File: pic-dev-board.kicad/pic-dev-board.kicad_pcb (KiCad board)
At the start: 2 copper layers, 100 x 100 mm, 0 parts

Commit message: initial pcb-layout, no traces yet
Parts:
- added ?: , , F.Cu at (34.5, 33.3)
- added C1: 100n, Capacitor_THT:C_Disc_D3.0mm_W2.0mm_P2.50mm, F.Cu at (54.0, 49.0)
- added D1: LED, user:LED_1206_3216_Pad1.7x1.75mm_BB, F.Cu at (109.2, 71.4)
- added D10: LED, user:LED_1206_3216_Pad1.7x1.75mm_BB, F.Cu at (82.0, 71.4)
- added D11: LED, user:LED_1206_3216_Pad1.7x1.75mm_BB, F.Cu at (79.5, 71.4)
- added D12: LED, user:LED_1206_3216_Pad1.7x1.75mm_BB, F.Cu at (77.0, 71.4)
- added D13: LED, user:LED_1206_3216_Pad1.7x1.75mm_BB, F.Cu at (74.4, 71.4)
- added D14: LED, user:LED_1206_3216_Pad1.7x1.75mm_BB, F.Cu at (71.9, 71.4)
- added D15: LED, user:LED_1206_3216_Pad1.7x1.75mm_BB, F.Cu at (65.8, 71.4)
- added D16: LED, user:LED_1206_3216_Pad1.7x1.75mm_BB, F.Cu at (63.2, 71.4)
- added D17: LED, user:LED_1206_3216_Pad1.7x1.75mm_BB, F.Cu at (60.7, 71.4)
- added D18: LED, user:LED_1206_3216_Pad1.7x1.75mm_BB, F.Cu at (58.2, 71.4)
- added D19: LED, user:LED_1206_3216_Pad1.7x1.75mm_BB, F.Cu at (55.6, 71.4)
- added D2: LED, user:LED_1206_3216_Pad1.7x1.75mm_BB, F.Cu at (109.2, 82.8)
- added D20: LED, user:LED_1206_3216_Pad1.7x1.75mm_BB, F.Cu at (53.2, 71.4)
- added D21: LED, user:LED_1206_3216_Pad1.7x1.75mm_BB, F.Cu at (50.5, 71.4)
- added D22: LED, user:LED_1206_3216_Pad1.7x1.75mm_BB, F.Cu at (48.0, 71.4)
- added D3: LED, user:LED_1206_3216_Pad1.7x1.75mm_BB, F.Cu at (109.2, 75.2)
- added D4: LED, user:LED_1206_3216_Pad1.7x1.75mm_BB, F.Cu at (109.2, 86.6)
- added D5: LED, user:LED_1206_3216_Pad1.7x1.75mm_BB, F.Cu at (109.2, 79.0)
- added D6: D_Schottky, Diode_THT:D_A-405_P7.62mm_Horizontal, F.Cu at (46.5, 55.1)
- added D7: LED, user:LED_1206_3216_Pad1.7x1.75mm_BB, F.Cu at (89.7, 71.4)
- added D8: LED, user:LED_1206_3216_Pad1.7x1.75mm_BB, F.Cu at (87.1, 71.4)
- added D9: LED, user:LED_1206_3216_Pad1.7x1.75mm_BB, F.Cu at (84.6, 71.4)
- added DS1: WC1602A, user:WC1602A_Connector, F.Cu at (47.0, 34.1)
- added J1: Conn_GP0, Connector_PinHeader_2.54mm:PinHeader_1x03_P2.54mm_Vertical, F.Cu at (99.6, 71.4)
- added J10: Jumper DATin, Connector_PinHeader_2.54mm:PinHeader_1x02_P2.54mm_Vertical, F.Cu at (96.5, 59.7)
- added J11: Conn_SR_2, Connector_PinHeader_2.54mm:PinHeader_1x08_P2.54mm_Vertical, F.Cu at (65.8, 87.4)
- added J12: Conn_SR_1, Connector_PinHeader_2.54mm:PinHeader_1x08_P2.54mm_Vertical, F.Cu at (89.7, 87.4)
- added J13: Conn_5V_GND, Connector_PinHeader_2.54mm:PinHeader_2x15_P2.54mm_Vertical, F.Cu at (80.8, 91.2)
- added J14: Jumper CLKin, Connector_PinHeader_2.54mm:PinHeader_1x02_P2.54mm_Vertical, F.Cu at (89.9, 59.4)
- added J15: Barrel_Jack_Switch, Connector_BarrelJack:BarrelJack_CUI_PJ-102AH_Horizontal, F.Cu at (44.0, 99.0)
- added J16: RUN/~PGM, Connector_PinHeader_2.54mm:PinHeader_1x02_P2.54mm_Vertical, F.Cu at (33.3, 56.0)
- added J17: I2C, Connector_PinHeader_2.54mm:PinHeader_1x04_P2.54mm_Vertical, F.Cu at (33.1, 64.0)
- added J18: GP1(RA1)/RB6, Connector_PinHeader_2.54mm:PinHeader_1x03_P2.54mm_Vertical, F.Cu at (59.0, 59.0)
- added J19: GP2(RA2)/RB4, Connector_PinHeader_2.54mm:PinHeader_1x03_P2.54mm_Vertical, F.Cu at (72.0, 59.0)
- added J2: Conn_GP4, Connector_PinHeader_2.54mm:PinHeader_1x03_P2.54mm_Vertical, F.Cu at (99.6, 82.8)
- added J3: Conn_GP1, Connector_PinHeader_2.54mm:PinHeader_1x03_P2.54mm_Vertical, F.Cu at (99.6, 75.2)
- added J4: Conn_GP5, Connector_PinHeader_2.54mm:PinHeader_1x03_P2.54mm_Vertical, F.Cu at (99.6, 86.6)
- added J5: Conn_GP2, Connector_PinHeader_2.54mm:PinHeader_1x03_P2.54mm_Vertical, F.Cu at (99.6, 79.0)
- added J6: Conn_ICSP, Connector_PinHeader_2.54mm:PinHeader_1x06_P2.54mm_Vertical, F.Cu at (33.3, 39.3)
- added J7: Conn_TRISC, Connector_PinHeader_2.54mm:PinHeader_1x10_P2.54mm_Vertical, F.Cu at (126.2, 97.8)
- added J8: Conn_TRISA, Connector_PinHeader_2.54mm:PinHeader_1x07_P2.54mm_Vertical, F.Cu at (126.2, 59.2)
- added J9: Conn_TRISB, Connector_PinHeader_2.54mm:PinHeader_1x06_P2.54mm_Vertical, F.Cu at (126.2, 79.8)
- added R1: 4.7k, user:R_1206_3216_Pad1.7x1.75mm_BB, F.Cu at (94.5, 71.4)
- added R10: 1k, user:R_1206_3216_Pad1.7x1.75mm_BB, F.Cu at (114.8, 79.0)
- added R11: 1k, user:R_1206_3216_Pad1.7x1.75mm_BB, F.Cu at (43.4, 52.8)
- added R12: 22k, user:R_1206_3216_Pad1.7x1.75mm_BB, F.Cu at (48.5, 51.8)
- added R13: 1k, user:R_1206_3216_Pad1.7x1.75mm_BB, F.Cu at (48.5, 48.5)
- added R14: 1k, user:R_1206_3216_Pad1.7x1.75mm_BB, F.Cu at (52.8, 45.0)
- added R15: 220, user:R_1206_3216_Pad1.7x1.75mm_BB, F.Cu at (90.4, 34.0)
- added R16: 4.7k, user:R_1206_3216_Pad1.7x1.75mm_BB, F.Cu at (36.6, 70.6)
- added R17: 4.7k, user:R_1206_3216_Pad1.7x1.75mm_BB, F.Cu at (36.6, 65.0)
- added R2: 1k, user:R_1206_3216_Pad1.7x1.75mm_BB, F.Cu at (114.8, 71.4)
- added R3: 4.7k, user:R_1206_3216_Pad1.7x1.75mm_BB, F.Cu at (94.5, 82.8)
- added R4: 1k, user:R_1206_3216_Pad1.7x1.75mm_BB, F.Cu at (114.8, 82.8)
- added R5: 4.7k, user:R_1206_3216_Pad1.7x1.75mm_BB, F.Cu at (94.5, 75.2)
- added R6: 1k, user:R_1206_3216_Pad1.7x1.75mm_BB, F.Cu at (114.8, 75.2)
- added R7: 4.7k, user:R_1206_3216_Pad1.7x1.75mm_BB, F.Cu at (94.5, 86.6)
- added R8: 1k, user:R_1206_3216_Pad1.7x1.75mm_BB, F.Cu at (114.8, 86.6)
- added R9: 4.7k, user:R_1206_3216_Pad1.7x1.75mm_BB, F.Cu at (94.5, 79.0)
- added REF**: Proto_Area_13x15_P2.54mm_Drill1.0mm, Proto_Area:Proto_Area_13x15, F.Cu at (85.9, 91.2)
- added REF**: Proto_Area_13x15_P2.54mm_Drill1.0mm, Proto_Area:Proto_Area_13x15, F.Cu at (47.8, 91.2)
- added REF**: MountingHole_2.7mm_M2.5, MountingHole:MountingHole_2.7mm_M2.5, F.Cu at (126.7, 33.3)
- added REF**: MountingHole_2.7mm_M2.5, MountingHole:MountingHole_2.7mm_M2.5, F.Cu at (126.7, 126.7)
- added REF**: MountingHole_2.7mm_M2.5, MountingHole:MountingHole_2.7mm_M2.5, F.Cu at (33.3, 126.7)
- added REF**: MountingHole_2.7mm_M2.5, MountingHole:MountingHole_2.7mm_M2.5, F.Cu at (33.3, 33.3)
- added RN1: 680, Resistor_THT:R_Array_SIP9, F.Cu at (92.2, 64.8)
- added RN2: 680, Resistor_THT:R_Array_SIP9, F.Cu at (68.3, 64.8)
- added RV1: 10K, Potentiometer_THT:Potentiometer_Bourns_3386X_Horizontal, F.Cu at (126.0, 49.0)
- added SW1: SW_Push, Button_Switch_THT:SW_PUSH_6mm_H9.5mm, F.Cu at (33.3, 90.9)
- added U1: PIC16F690-IP, Package_DIP:DIP-20_W7.62mm_Socket, F.Cu at (58.0, 53.0)
- added U2: 74HC595, Package_DIP:DIP-16_W7.62mm_Socket, F.Cu at (89.7, 76.2)
- added U3: 74HC595, Package_DIP:DIP-16_W7.62mm_Socket, F.Cu at (65.8, 76.2)

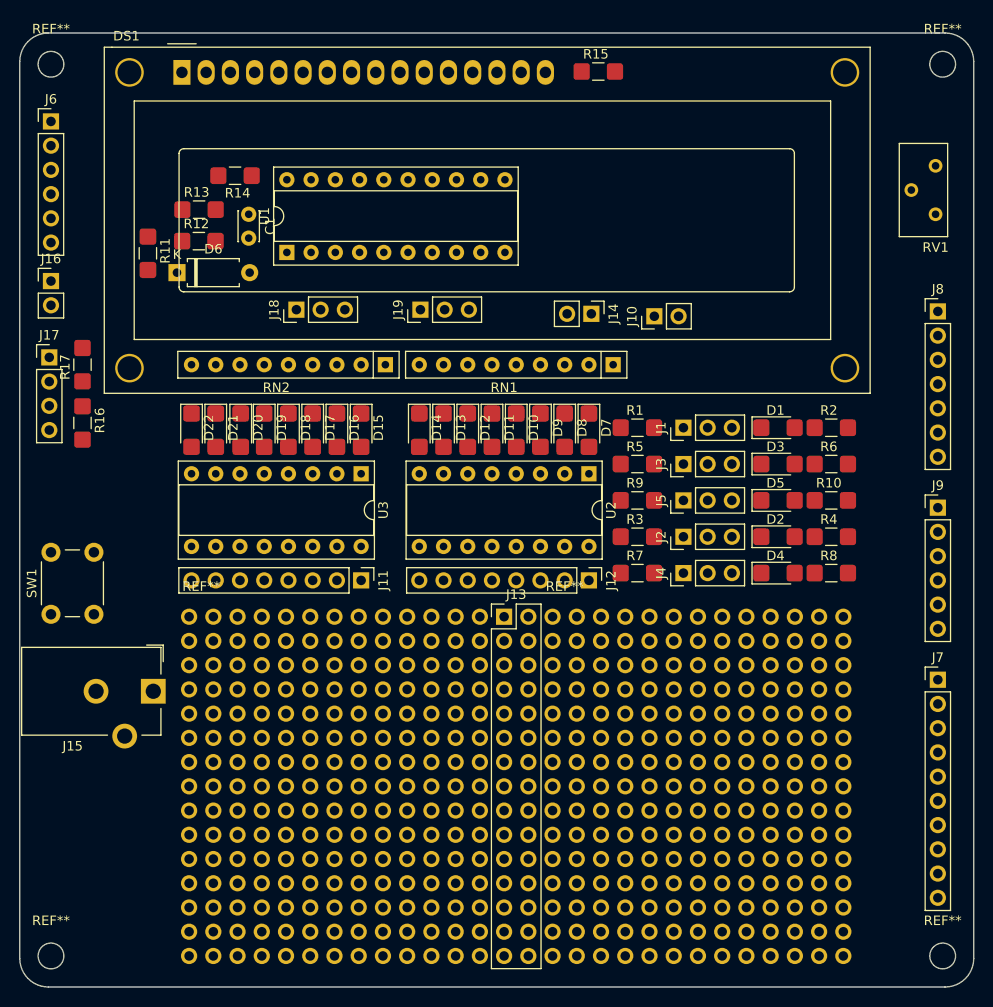
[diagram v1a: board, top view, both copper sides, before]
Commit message: added ground-planes
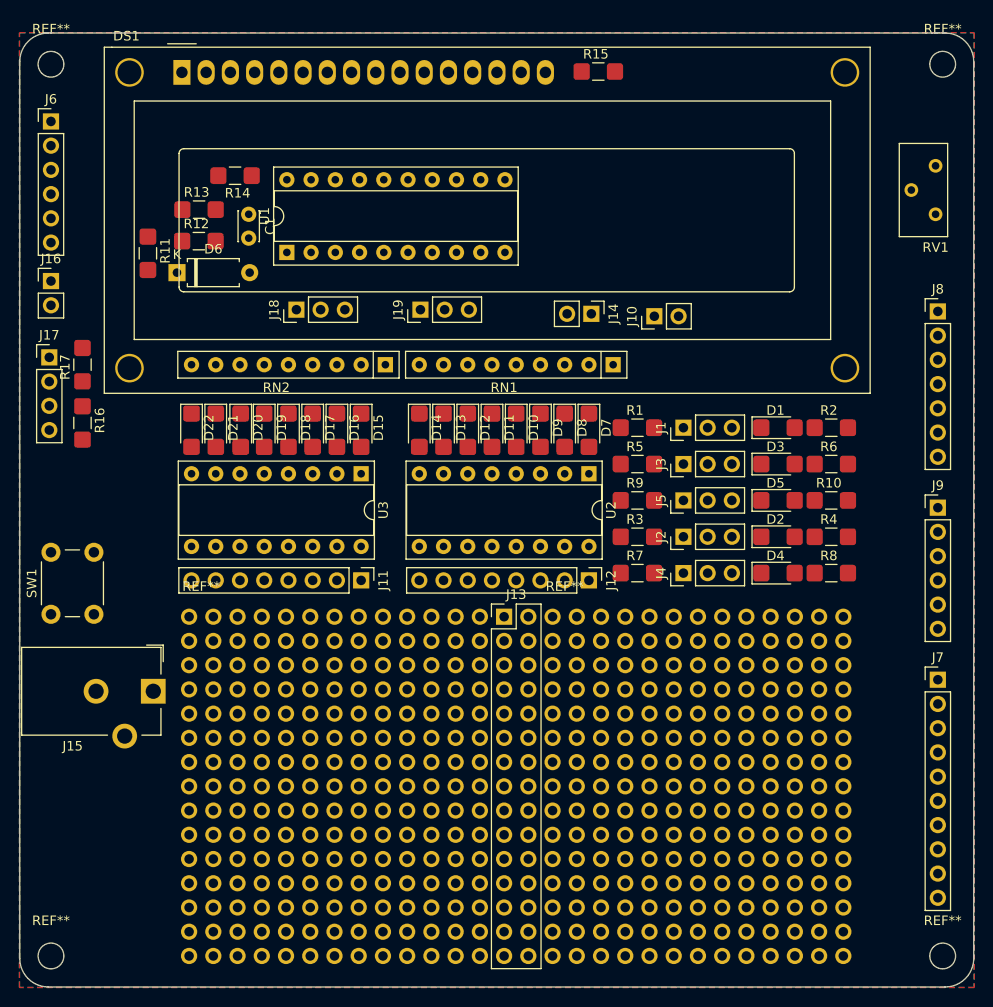
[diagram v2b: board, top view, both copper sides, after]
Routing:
- added copper zone on B.Cu, net GND
- added copper zone on F.Cu, net GND
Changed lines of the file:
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@@
   (gr_line (start 30 33) (end 30 127) (layer Edge.Cuts) (width 0.1))
   (gr_line (start 33 130) (end 127 130) (layer Edge.Cuts) (width 0.1))
+  (zone (net 2) (net_name GND) (layer F.Cu) (hatch edge 0.508)
+    (connect_pads (clearance 0.508))
+    (min_thickness 0.254)
+    (fill yes (arc_segments 32) (thermal_gap 0.508) (thermal_bridge_width 0.508))
+    (polygon
+      (pts
+        (xy 130.048 130.048) (xy 29.972 130.048) (xy 29.972 29.972) (xy 130.048 29.972)
+      )
+    )
+  )
+  (zone (net 2) (net_name GND) (layer B.Cu) (hatch edge 0.508)
+    (connect_pads (clearance 0.508))
+    (min_thickness 0.254)
+    (fill yes (arc_segments 32) (thermal_gap 0.508) (thermal_bridge_width 0.508))
+    (polygon
+      (pts
+        (xy 130.048 130.048) (xy 29.972 130.048) (xy 29.972 29.972) (xy 130.048 29.972)
+      )
+    )
+  )
 )

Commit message: finished traces
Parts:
- moved J8 44.7 mm to (125.2, 103.9)
- moved J7 41.7 mm to (125.2, 56.1)
- moved R15 32.9 mm to (123.0, 37.9)
- moved J9 6.68 mm to (125.2, 86.4)
- moved R13 0.76 mm to (48.5, 49.3)
- moved J4 0.23 mm to (99.3, 86.6)
- moved J2 0.20 mm to (99.4, 82.8)
- moved J1 0.18 mm to (99.4, 71.4)
- moved J3 0.18 mm to (99.4, 75.2)
- moved J5 0.18 mm to (99.4, 79.0)
- turned D1 to 180 degrees
- turned D2 to 180 degrees
- turned D3 to 180 degrees
- turned D4 to 180 degrees
- turned D5 to 180 degrees
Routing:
- net +5V: track 0.00 -> 358.4 mm, vias 0 -> 1
- net /GP0: track 0.00 -> 139.8 mm, vias 0 -> 2
- net /RB6: track 0.00 -> 125.6 mm, vias 0 -> 1
- net /GP2: track 0.00 -> 115.7 mm, vias 0 -> 2
- net /GP5: track 0.00 -> 114.7 mm, vias 0 -> 1
- net /GP1: track 0.00 -> 114.7 mm
- net /GP4: track 0.00 -> 112.4 mm
- net /RB4: track 0.00 -> 111.1 mm, vias 0 -> 1
- net /RB5: track 0.00 -> 93.7 mm, vias 0 -> 1
- net Net-(DS1-Pad3): track 0.00 -> 86.2 mm
- net /RB7: track 0.00 -> 83.6 mm, vias 0 -> 1
- net /RC5: track 0.00 -> 80.4 mm
- net /RC0: track 0.00 -> 78.8 mm
- net /RC1: track 0.00 -> 76.8 mm
- net /RS: track 0.00 -> 76.4 mm, vias 0 -> 1
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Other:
- net class power added: clearance 0.2, trace_width 0.5, via_dia 0.8, via_drill 0.4
